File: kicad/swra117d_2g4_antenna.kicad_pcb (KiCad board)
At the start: 2 copper layers, 40 x 30 mm, 2 parts, among them J1 SMA edge launch

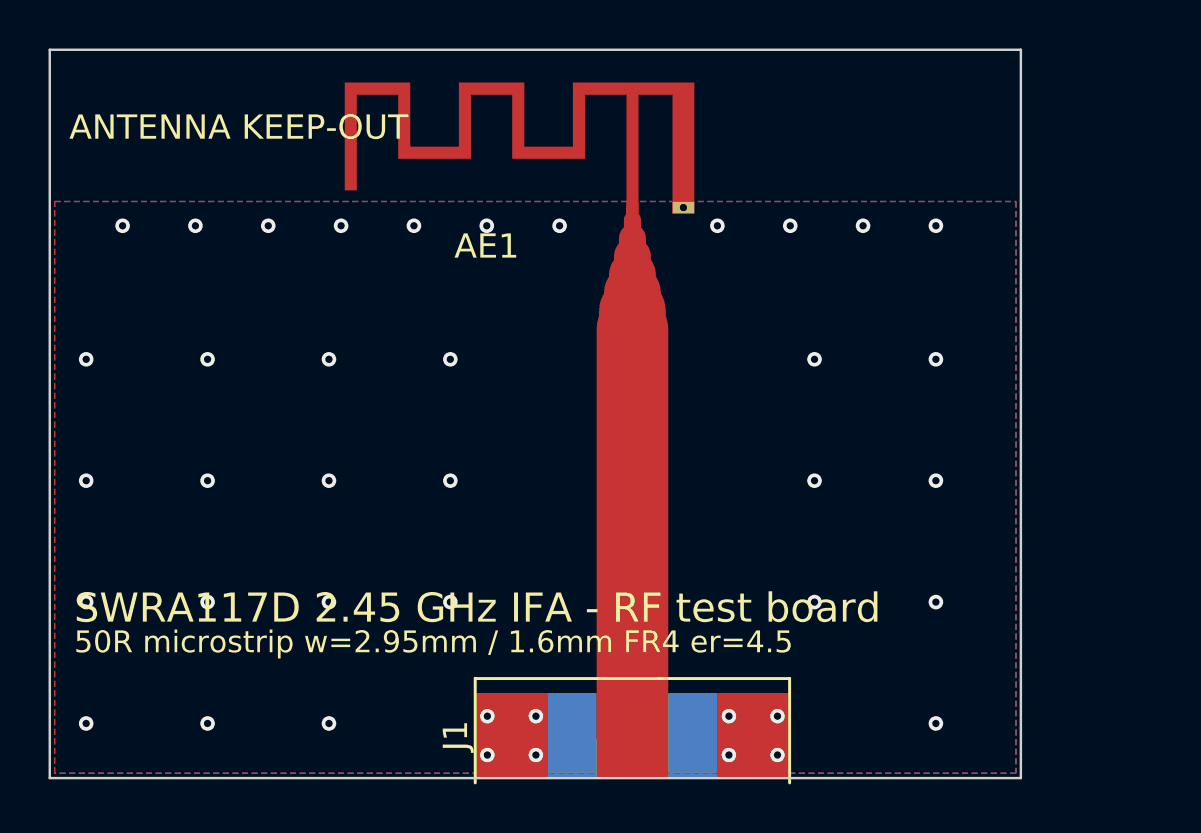
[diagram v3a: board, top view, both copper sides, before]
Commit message: Pi network on the first board: pads, and a 0 ohm link
Asked for the matching components, with the condition "if 50 ohm matching is
mandatory".  It is not mandatory as values and there are none to fit:
SWRA117D says the antenna is already a 50 ohm design and publishes no matching
BOM.  Inventing an L and a C would repeat the 0.8 nH this project already got
wrong once by fitting it to its own model.

What AN058 section 3.4 actually asks for is the network to exist: "If the
antenna design is adequately matched then it just takes one zero ohm resistor
or DC block cap to be inserted into the pi-matching network."  So that is what
is fitted:

  Z2  0R     series - the link.  100 pF is the drop-in where the radio needs
             DC isolation, which this antenna's DC short to ground makes worth
             checking
  Z1  DNP    shunt, connector side
  Z3  DNP    shunt, antenna side

Z1 and Z3 exist because AN058's own measurements show an enclosure only ever
pulls resonance down, and a board with nowhere to compensate gets respun.

Three problems the checkers found on the way, all real:

  * A 2.95 mm track cannot butt onto an 0402 land.  KiCad tracks are
    round-capped, so the cap bulges 1.475 mm past the endpoint and lands
    across the opposite pad, 0.96 mm away - KiCad's own DRC would have said
    so too.  Necking the line down is worse: 0.6 mm is ~100 ohm here and the
    6.5 mm to taper down and back is 3.8 nH, j58 ohm at 2.45 GHz, in series
    with the antenna.  So the series land is widened to the line instead
    (Chip_0402_RF_WideLand: 0402 pitch, 2.95 mm pads) and the wide line stops
    2.0 mm short so its cap reaches into its own pad and clears the other.
    The shunts keep the ordinary land on a 0.6 mm stub, which is not in the
    through path.
  * check_feed_width had been taking the last non-GND pad it saw as the port,
    which the new 0402s took over.  It now looks for the footprint that brings
    its own B.Cu reference copper - which is what a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
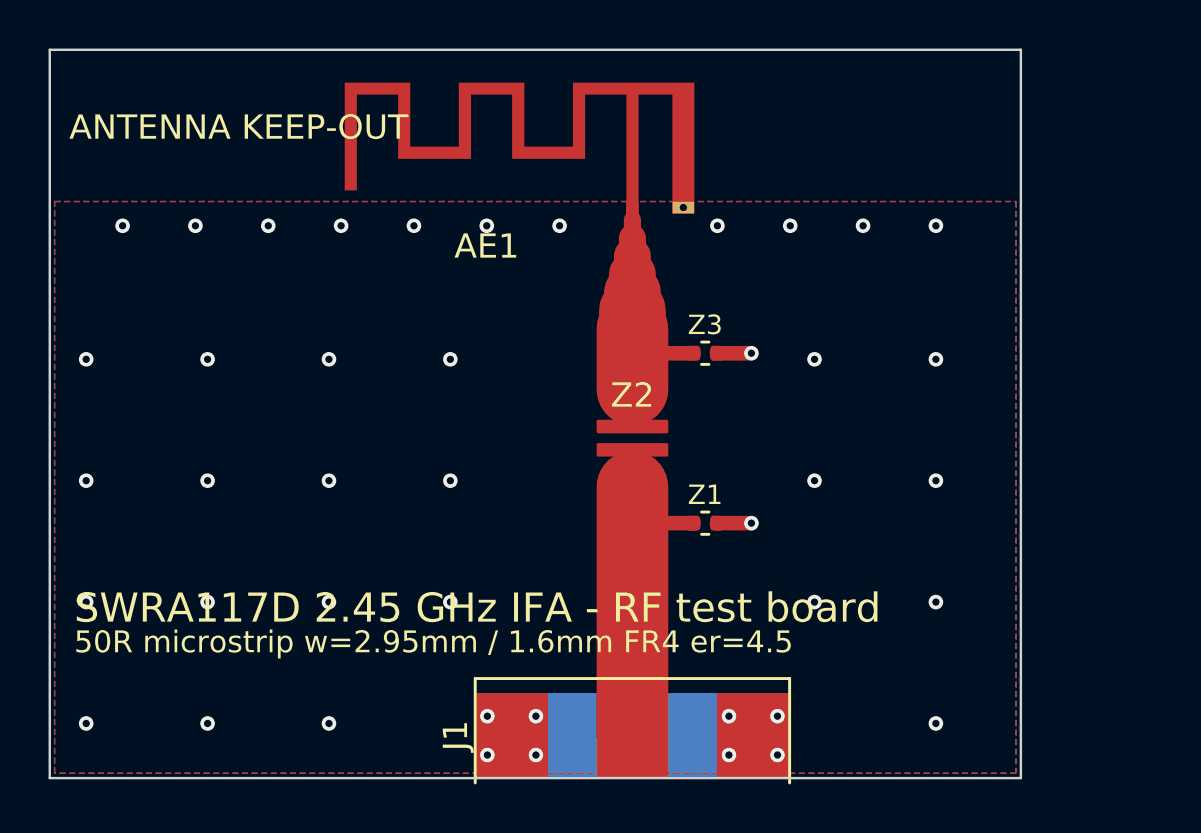
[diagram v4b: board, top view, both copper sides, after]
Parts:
- added Z1: DNP, SWRA117D_RF:Chip_0402_1005Metric_RF, F.Cu at (127.0, 79.5)
- added Z2: 0R, SWRA117D_RF:Chip_0402_RF_WideLand, F.Cu at (124.0, 76.0)
- added Z3: DNP, SWRA117D_RF:Chip_0402_1005Metric_RF, F.Cu at (127.0, 72.5)
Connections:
- J1 pad 1: ANT_FEED -> RF_IN
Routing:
- net RF_IN: track 0.00 -> 12.8 mm
- net ANT_FEED: track 21.8 -> 10.0 mm
- net GND: track 0.00 -> 2.84 mm, vias 41 -> 43
